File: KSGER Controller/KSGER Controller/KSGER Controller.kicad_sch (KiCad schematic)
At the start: 51 parts

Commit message: Updated C10 and C11 to 1nF
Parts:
- C10, C11: JCLPCB Part # C49678 -> C46653
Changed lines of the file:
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@@
       (effects (font (size 1.27 1.27)) hide)
     )
-    (property "Value" "" (id 1) (at 88.9 31.75 0))
+    (property "Value" "PWR_FLAG" (id 1) (at 88.9 31.75 0))
     (property "Footprint" "" (id 2) (at 88.9 36.83 0)
       (effects (font (size 1.27 1.27)) hide)
@@
       (effects (font (size 1.27 1.27)) hide)
     )
-    (property "JCLPCB Part #" "C49678" (id 4) (at 104.14 252.73 0)
+    (property "JCLPCB Part #" "C46653" (id 4) (at 104.14 252.73 0)
       (effects (font (size 1.27 1.27)) hide)
     )
@@
       (effects (font (size 1.27 1.27)) hide)
     )
-    (property "JCLPCB Part #" "C49678" (id 4) (at 111.76 252.73 0)
+    (property "JCLPCB Part #" "C46653" (id 4) (at 111.76 252.73 0)
       (effects (font (size 1.27 1.27)) hide)
     )
@@
       (effects (font (size 1.27 1.27)) hide)
     )
-    (property "Value" "" (id 1) (at 302.26 182.88 0))
+    (property "Value" "PWR_FLAG" (id 1) (at 302.26 182.88 0))
     (property "Footprint" "" (id 2) (at 302.26 177.8 0)
       (effects (font (size 1.27 1.27)) hide)
@@
       (effects (font (size 1.27 1.27)) hide)
     )
-    (property "Value" "" (id 1) (at 317.5 78.74 0))
+    (property "Value" "PWR_FLAG" (id 1) (at 317.5 78.74 0))
     (property "Footprint" "" (id 2) (at 317.5 83.82 0)
       (effects (font (size 1.27 1.27)) hide)
@@
       (effects (font (size 1.27 1.27)) hide)
     )
-    (property "Value" "" (id 1) (at 85.09 104.14 0))
+    (property "Value" "PWR_FLAG" (id 1) (at 85.09 104.14 0))
     (property "Footprint" "" (id 2) (at 85.09 109.22 0)
       (effects (font (size 1.27 1.27)) hide)
@@
     )
     (path "/34211a8b-f6dd-4654-bd6c-8b272efe5d87"
-      (reference "C10") (unit 1) (value "0.1") (footprint "Capacitor_SMD:C_0805_2012Metric")
+      (reference "C10") (unit 1) (value "0.001") (footprint "Capacitor_SMD:C_0805_2012Metric")
     )
     (path "/3f5ab397-d624-497a-a1c4-ba34693fdb0b"
-      (reference "C11") (unit 1) (value "0.1") (footprint "Capacitor_SMD:C_0805_2012Metric")
+      (reference "C11") (unit 1) (value "0.001") (footprint "Capacitor_SMD:C_0805_2012Metric")
     )
     (path "/e98d8a8a-11e1-427f-aad2-792b970d9535"

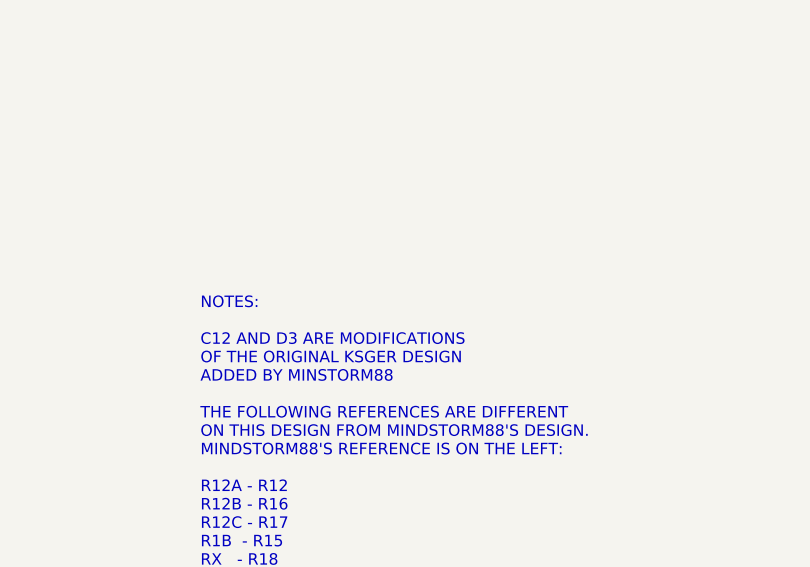
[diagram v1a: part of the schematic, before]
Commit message: Added cap value note
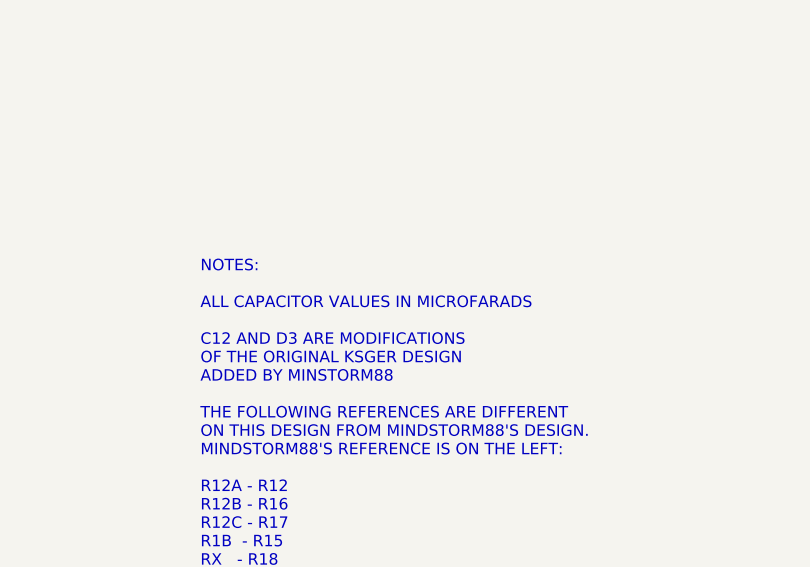
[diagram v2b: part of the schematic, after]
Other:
- note added: "NOTES: ALL CAPACITOR VALUES IN MICROFARADS C12 AND D3 ARE MODIFICATIONS OF THE ORIGINAL KSGER DESIGN ADDED BY MINSTORM88 THE FOLLOWING REFERENCES ARE DIFFERENT ON THIS DESIGN FROM MINDSTORM88'S DESIGN. MINDSTORM88'S REFERENCE IS ON THE LEFT: R12A - R12 R12B - R16 R12C - R17 R1B - R15 RX - R18 R10 - THERE ARE 3 RESISTORS MARKED AS R10 ON THE ORIGINAL BOARD. TO STOP KICAD FROM THROWING AN ANNOTATIO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"
- note removed: "NOTES: C12 AND D3 ARE MODIFICATIONS OF THE ORIGINAL KSGER DESIGN ADDED BY MINSTORM88 THE FOLLOWING REFERENCES ARE DIFFERENT ON THIS DESIGN FROM MINDSTORM88'S DESIGN. MINDSTORM88'S REFERENCE IS ON THE LEFT: R12A - R12 R12B - R16 R12C - R17 R1B - R15 RX - R18 R10 - THERE ARE 3 RESISTORS MARKED AS R10 ON THE ORIGINAL BOARD. TO STOP KICAD FROM THROWING AN ANNOTATION ERROR, I HAVE RENAMED TWO OF THEM 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"
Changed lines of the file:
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@@
     (effects (font (size 1.27 1.27)) (justify left bottom))
   )
-  (text "NOTES:\n\nC12 AND D3 ARE MODIFICATIONS\nOF THE ORIGINAL KSGER DESIGN\nADDED BY MINSTORM88\n\nTHE FOLLOWING REFERENCES ARE DIFFERENT\nON THIS DESIGN FROM MINDSTORM88'S DESIGN.\nMINDSTORM88'S REFERENCE IS ON THE LEFT:\n\nR12A - R12\nR12B - R16\nR12C - R17\nR1B  - R15\nRX   - R18\n\nR10 - THERE ARE 3 RESISTORS MARKED AS R10 ON\nTHE ORIGINAL BOARD.  TO STOP KICAD FROM THROWING\nAN ANNOTATION ERROR, I HAVE RENAMED TWO OF \nTHEM TO R19 AND R20."
+  (text "NOTES:\n\nALL CAPACITOR VALUES IN MICROFARADS\n\nC12 AND D3 ARE MODIFICATIONS\nOF THE ORIGINAL KSGER DESIGN\nADDED BY MINSTORM88\n\nTHE FOLLOWING REFERENCES ARE DIFFERENT\nON THIS DESIGN FROM MINDSTORM88'S DESIGN.\nMINDSTORM88'S REFERENCE IS ON THE LEFT:\n\nR12A - R12\nR12B - R16\nR12C - R17\nR1B  - R15\nRX   - R18\n\nR10 - THERE ARE 3 RESISTORS MARKED AS R10 ON\nTHE ORIGINAL BOARD.  TO STOP KICAD FROM THROWING\nAN ANNOTATION ERROR, I HAVE RENAMED TWO OF \nTHEM TO R19 AND R20."
     (at 233.68 279.4 0)
     (effects (font (size 1.27 1.27)) (justify left bottom))
